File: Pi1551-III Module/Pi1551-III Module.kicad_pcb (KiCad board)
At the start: 2 copper layers, 100 x 100 mm, 25 parts, among them J1 DC IN, J2 C64_IEC, J3 C64_IEC, J8 Module_Panel, M1 Mounting, M2 Mounting, M3 Mounting, M4 Mounting, U1 7406

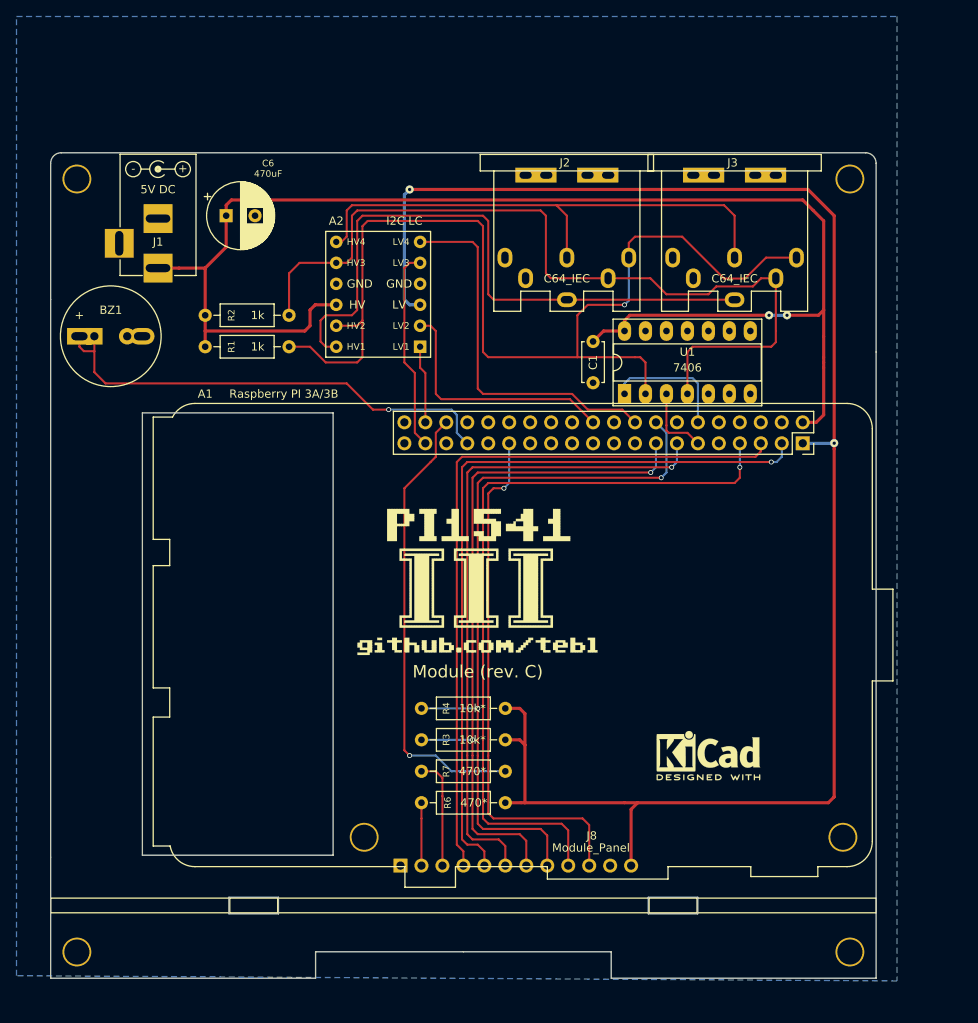
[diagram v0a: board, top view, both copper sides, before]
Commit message: PI1551 branding and Microgramma font labels
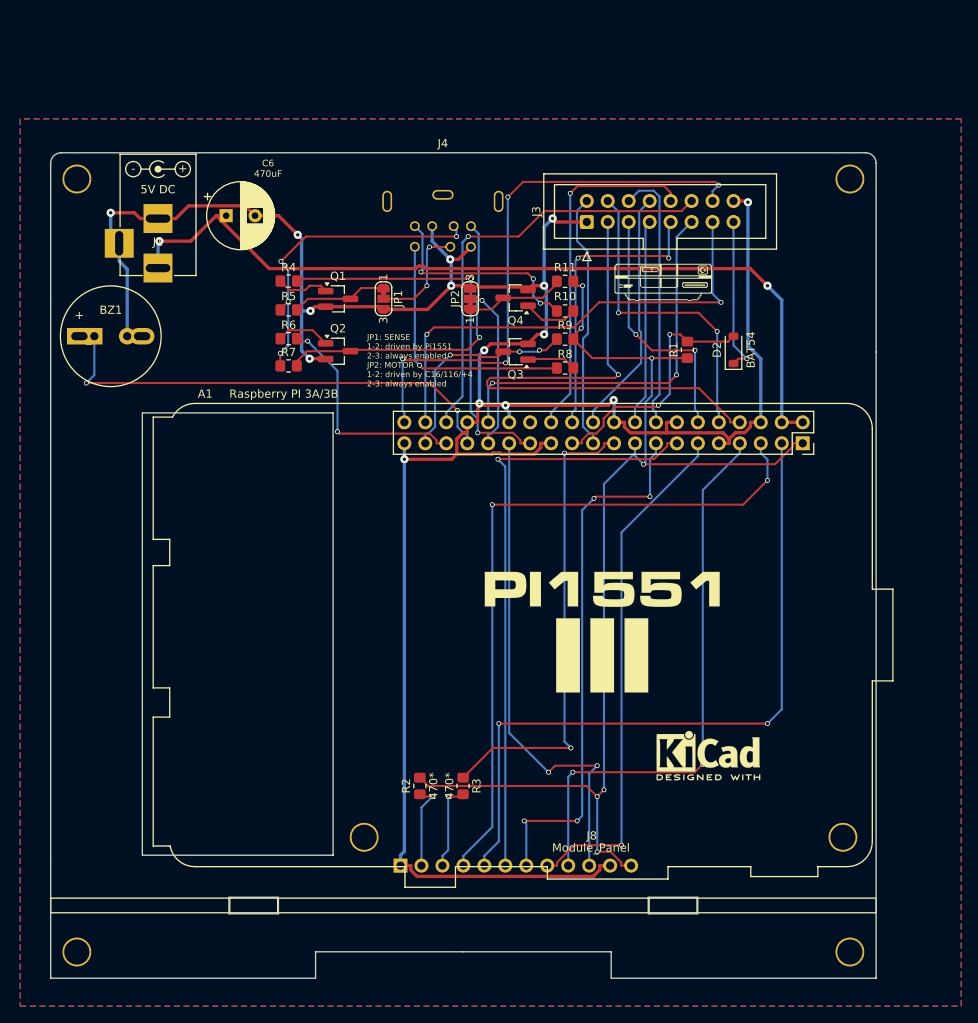
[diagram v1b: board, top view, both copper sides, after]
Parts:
- removed A2: I2C LC, IIC_4CH_Level_Converter:4CH_I2C_Level_Converter
- removed C1: 100nF, Capacitor_THT:C_Disc_D4.7mm_W2.5mm_P5.00mm
- removed G***: LOGO, pi1541:Pi1541-logo3
- removed J2: C64_IEC, C64_IEC:DIN6_IEC
- removed U1: 7406, Package_DIP:DIP-14_W7.62mm_Socket_LongPads
- added D2: BAT54, Diode_SMD:D_SOD-123, F.Cu at (152.9, 78.5)
- added J4: Mini-DIN-7, Conn_DIN_round:Mini_DIN_round_7_canned, F.Cu at (117.7, 55.0)
- added JP1: SolderJumper_3_Bridged12, Jumper:SolderJumper-3_P1.3mm_Bridged12_RoundedPad1.0x1.5mm_NumberLabels, F.Cu at (110.5, 72.3)
- added JP2: SolderJumper_3_Bridged12, Jumper:SolderJumper-3_P1.3mm_Bridged12_RoundedPad1.0x1.5mm_NumberLabels, F.Cu at (121.0, 72.3)
- added Q1: MMBT3904, Package_TO_SOT_SMD:SOT-23_Handsoldering, F.Cu at (105.0, 72.3)
- added Q2: MMBT3904, Package_TO_SOT_SMD:SOT-23_Handsoldering, F.Cu at (105.0, 78.7)
- added Q3: MMBT3904, Package_TO_SOT_SMD:SOT-23_Handsoldering, F.Cu at (126.5, 78.7)
- added Q4: MMBT3904, Package_TO_SOT_SMD:SOT-23_Handsoldering, F.Cu at (126.5, 72.2)
- added R10: 10k, Resistor_SMD:R_0805_2012Metric_Pad1.20x1.40mm_HandSolder, F.Cu at (132.5, 73.8)
- added R11: 10k, Resistor_SMD:R_0805_2012Metric_Pad1.20x1.40mm_HandSolder, F.Cu at (132.5, 70.2)
- added R5: 10k, Resistor_SMD:R_0805_2012Metric_Pad1.20x1.40mm_HandSolder, F.Cu at (99.0, 73.6)
- added R8: 10k, Resistor_SMD:R_0805_2012Metric_Pad1.20x1.40mm_HandSolder, F.Cu at (132.5, 80.7)
- added R9: 10k, Resistor_SMD:R_0805_2012Metric_Pad1.20x1.40mm_HandSolder, F.Cu at (132.5, 77.2)
- added kibuzzard-69864AC5: G***, kibuzzard-69864AC5, F.Cu at (137.0, 107.5)
- added kibuzzard-69864AE8: G***, kibuzzard-69864AE8, F.Cu at (137.0, 115.5)
- J3: value C64_IEC -> TCBM; footprint C64_IEC:DIN6_IEC -> Connector_IDC:IDC-Header_2x08_P2.54mm_Vertical
- Pi1541-drive: moved to F.Cu
- R1: value 1k -> 10k; footprint resistor:R_Axial_DIN0207_L6.3mm_D2.5mm_P10.16mm_Horizontal -> Resistor_SMD:R_0805_2012Metric_Pad1.20x1.40mm_HandSolder
- R2: value 1k -> 470*; footprint resistor:R_Axial_DIN0207_L6.3mm_D2.5mm_P10.16mm_Horizontal -> Resistor_SMD:R_0805_2012Metric_Pad1.20x1.40mm_HandSolder
- R3: value 10k* -> 470*; footprint resistor:R_Axial_DIN0207_L6.3mm_D2.5mm_P10.16mm_Horizontal -> Resistor_SMD:R_0805_2012Metric_Pad1.20x1.40mm_HandSolder
- R4: value 10k* -> 10k; footprint resistor:R_Axial_DIN0207_L6.3mm_D2.5mm_P10.16mm_Horizontal -> Resistor_SMD:R_0805_2012Metric_Pad1.20x1.40mm_HandSolder
- R6, R7: value 470* -> 10k; footprint resistor:R_Axial_DIN0207_L6.3mm_D2.5mm_P10.16mm_Horizontal -> Resistor_SMD:R_0805_2012Metric_Pad1.20x1.40mm_HandSolder
- moved R2 62.7 mm to (114.9, 131.3), turned to 90 degrees
- moved R6 58.5 mm to (99.0, 77.1)
- moved R1 58.4 mm to (147.3, 78.5), turned to 90 degrees
- moved R4 58.0 mm to (99.0, 70.2), turned to 0 degrees
- moved R7 55.7 mm to (99.0, 80.4), turned to 0 degrees
- moved Pi1541-drive 23.2 mm to (138.0, 66.4), turned to 0 degrees
- moved J3 18.4 mm to (135.1, 63.0), turned to 90 degrees
- moved R3 7.58 mm to (120.1, 131.3), turned to -90 degrees
- renumbered REF*** to REF1, REF*** to REF2
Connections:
- A1 pad 1: +3V3 -> +3.3V
- A1 pad 10: (no net) -> /DIO2
- A1 pad 11: RPI_CLK_OUT -> SW3_DOWN
- A1 pad 12: RPI_DATA_OUT -> /DIO3
- A1 pad 16: SW3_DOWN -> /DIO4
- A1 pad 17: (no net) -> +3.3V
- A1 pad 18: RPI_ATN -> /DIO5
- A1 pad 19: (no net) -> RPI_LED
- A1 pad 21: (no net) -> /DEV
- A1 pad 22: RPI_DATA_IN -> /DIO6
- A1 pad 23: (no net) -> /~{RESET_3V3}
- A1 pad 24: (no net) -> /DIO7
- A1 pad 26: (no net) -> /DIO8
- A1 pad 27: (no net) -> /TAP_SENSE
- A1 pad 28: (no net) -> unconnected-(A1-ID_SC/GPIO1-Pad28)
- A1 pad 31: (no net) -> /TAP_MOTOR
- A1 pad 32: (no net) -> /DAV
- A1 pad 35: (no net) -> /TAP_READ
- A1 pad 36: RPI_LED -> /STATUS0
- A1 pad 37: RPI_CLK_IN -> /TAP_WRITE
- A1 pad 38: RPI_RST -> /ACK
- A1 pad 4: (no net) -> +5V
- A1 pad 40: (no net) -> /STATUS1
- A1 pad 8: (no net) -> /DIO1
- J3 pad 1: (no net) -> GND
- J3 pad 2: GND -> /DEV
- J3 pad 3: C64_ATN -> /DIO1
- J3 pad 4: C64_CLK -> /DIO2
- J3 pad 5: C64_DATA -> /DIO3
- J3 pad 6: C64_RST -> /DIO4
- J3 pad 7: GND -> /DIO5
- J8 pad 12: +3V3 -> +3.3V
- R1 pad 1: +5V -> +3.3V
- R1 pad 2: C64_DATA -> /~{RESET_3V3}
- R2 pad 1: +5V -> LED_PWR
- R2 pad 2: C64_CLK -> +3.3V
- R3 pad 1: +3V3 -> RPI_LED
- R3 pad 2: SW2_UP -> LED_ACT
- R4 pad 1: +3V3 -> Net-(Q1-B)
- R4 pad 2: SW3_DOWN -> /TAP_SENSE
- R6 pad 1: LED_PWR -> Net-(Q2-B)
- R6 pad 2: +3V3 -> /TAP_READ
- R7 pad 1: RPI_LED -> /VCC_5V
- R7 pad 2: LED_ACT -> /CAS_READ
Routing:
- net GND: track 1.81 -> 319.0 mm, vias 0 -> 15
- net +3V3: track 206.9 -> 0.00 mm, vias 2 -> 0
- net +3.3V: track 0.00 -> 137.5 mm, vias 0 -> 7
- net C64_DATA: track 126.5 -> 0.00 mm, vias 1 -> 0
- net C64_CLK: track 103.3 -> 0.00 mm
- net C64_RST: track 75.9 -> 0.00 mm
- net +5V: track 172.6 -> 103.1 mm
- net /STATUS1: track 0.00 -> 69.4 mm, vias 0 -> 4
- net /DIO1: track 0.00 -> 68.4 mm, vias 0 -> 1
- net C64_ATN: track 64.4 -> 0.00 mm
- net /ACK: track 0.00 -> 58.1 mm, vias 0 -> 2
- net /STATUS0: track 0.00 -> 52.5 mm, vias 0 -> 1
- net /TAP_SENSE: track 0.00 -> 47.3 mm, vias 0 -> 2
- net /DAV: track 0.00 -> 47.0 mm, vias 0 -> 2
- net RPI_ATN: track 45.1 -> 0.00 mm
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- added copper zone on F.Cu, net GND
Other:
- board text added: "JP1: SENSE 1-2: driven by Pi1551 2-3: always enabled JP2: MOTOR 1-2: driven by C16/116/+4 2-3: always enabled"
- board text removed: "IEC1"
- board text removed: "IEC2"
- board text removed: "Module (rev. C)"

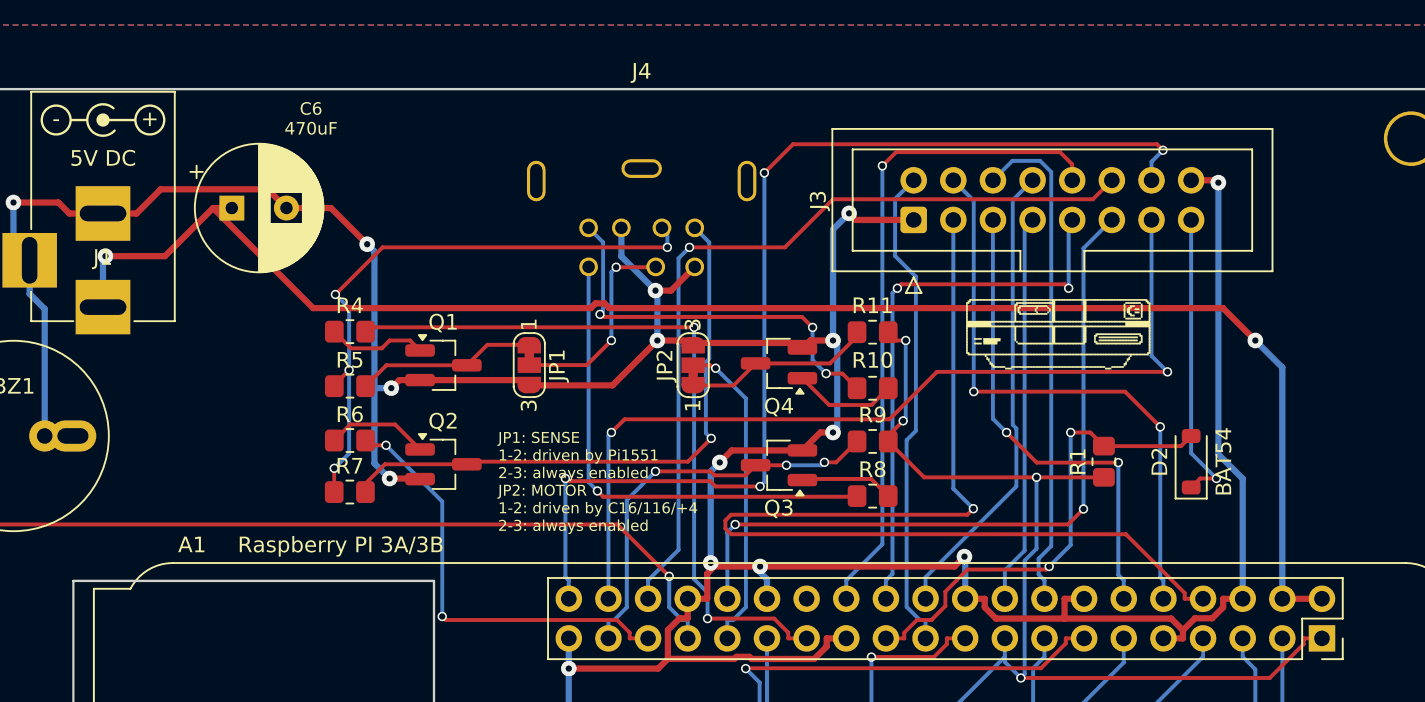
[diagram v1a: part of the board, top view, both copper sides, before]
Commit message: all 10K resistors to 3.3K, JLPCB part numbers for 470R resistors, 1.2mm track width for 5V - as short as possible
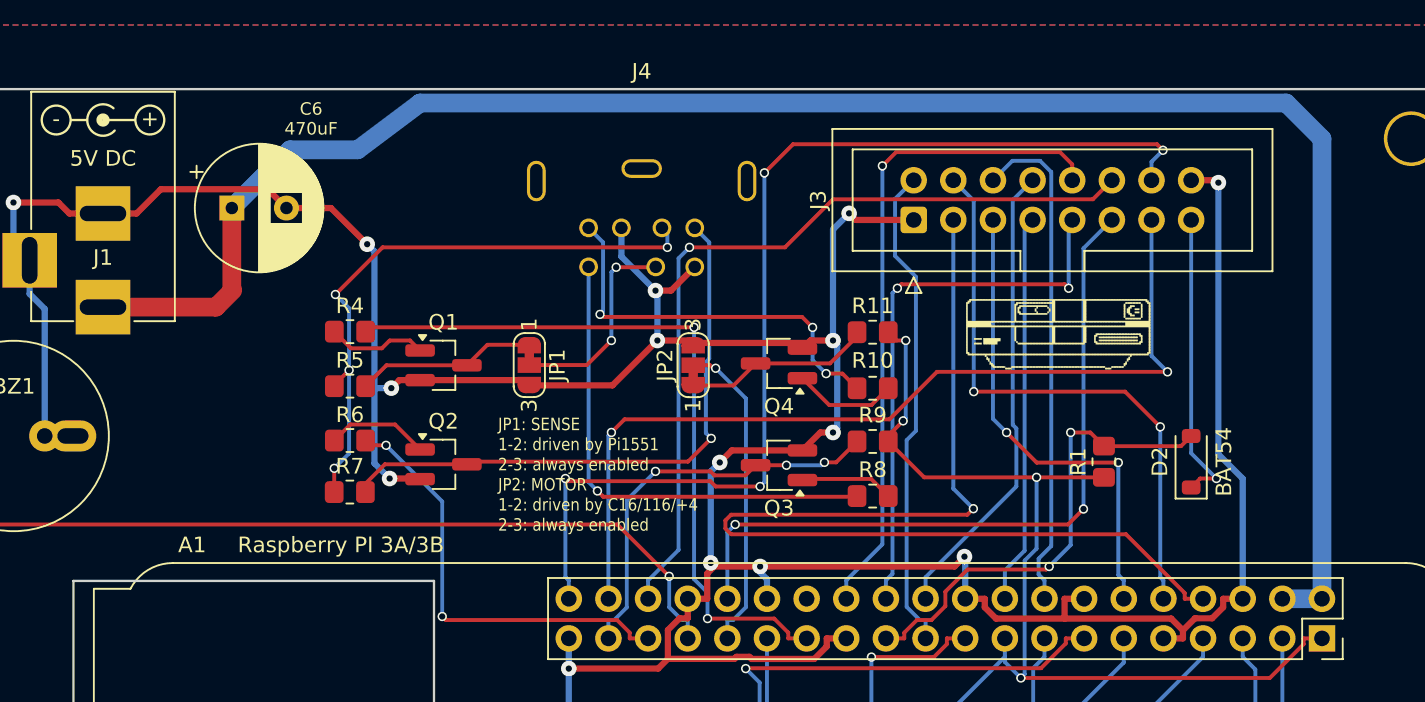
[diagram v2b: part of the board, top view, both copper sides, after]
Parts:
- R1, R10, R11, R4, R5, R6, R7, R8, R9: value 10k -> 3.3K
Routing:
- net +5V: track 103.1 -> 119.3 mm, vias 2 -> 0
